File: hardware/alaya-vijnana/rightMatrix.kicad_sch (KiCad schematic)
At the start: 42 parts, among them SW24 MX HotSwap, SW25 MX HotSwap, SW26 MX HotSwap, SW27 MX HotSwap, SW28 MX HotSwap, SW29 MX HotSwap, SW30 MX HotSwap, SW31 MX HotSwap, SW32 MX HotSwap, SW33 MX HotSwap, SW34 MX HotSwap, SW35 MX HotSwap, SW36 MX HotSwap, SW37 MX HotSwap, SW38 MX HotSwap, SW39 MX HotSwap, SW40 MX HotSwap, SW41 MX HotSwap, SW42 MX HotSwap, SW43 MX HotSwap, SW44 MX HotSwap

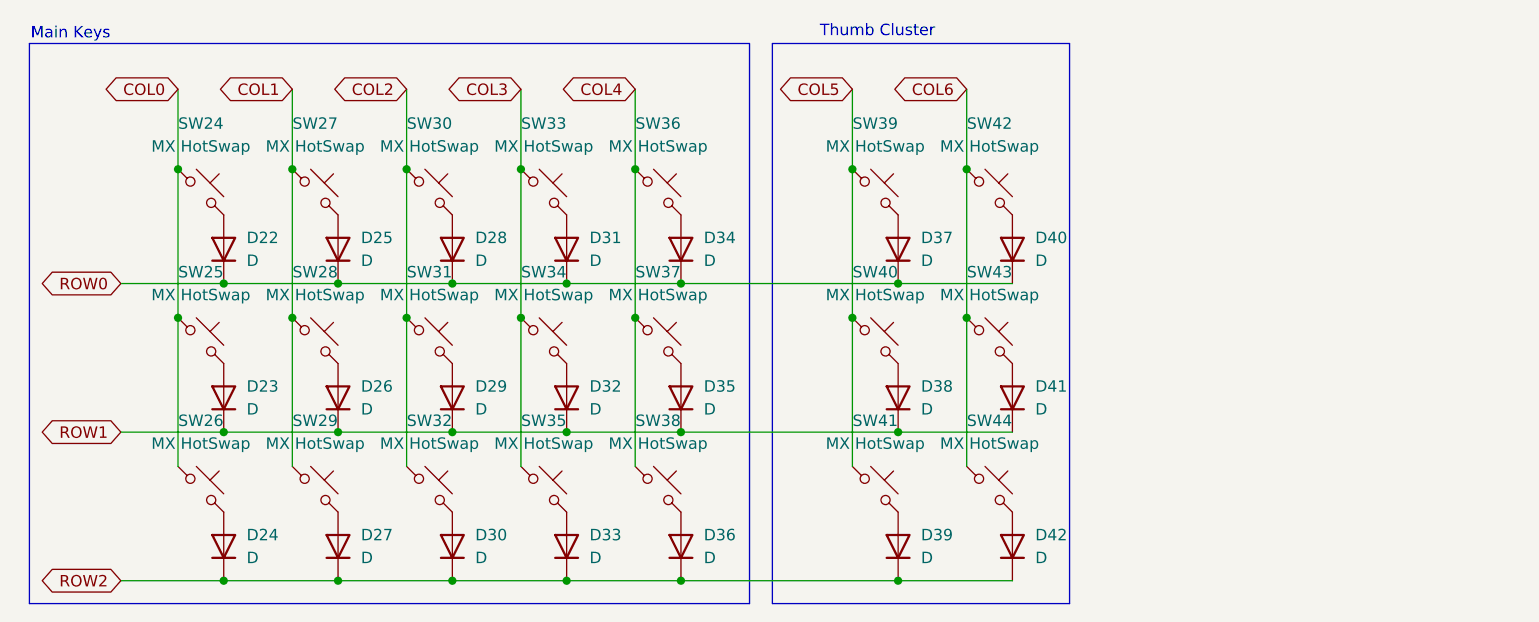
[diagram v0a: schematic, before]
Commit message: finished key wiring w/ connectors
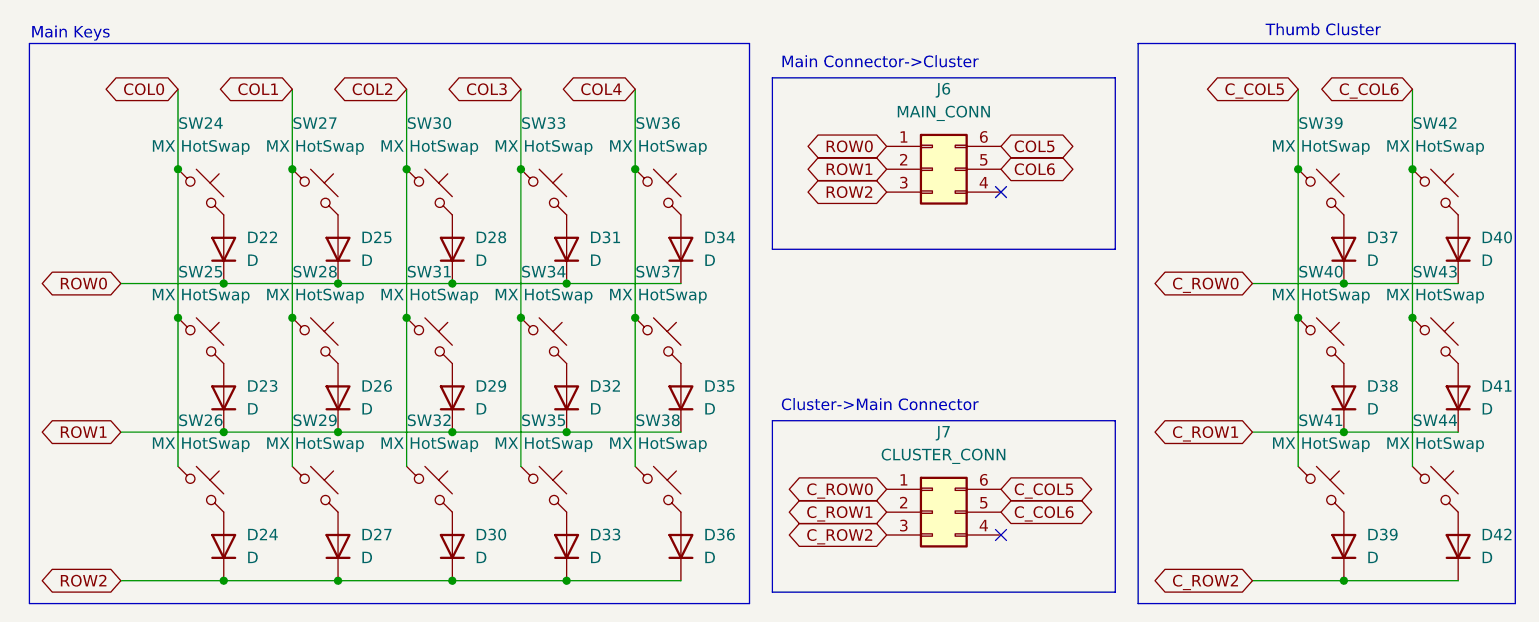
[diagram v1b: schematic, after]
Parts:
- added J6: MAIN_CONN, Connector_IDC:IDC-Header_2x03_P2.54mm_Horizontal, symbol Connector_Generic:Conn_02x03_Counter_Clockwise
- added J7: CLUSTER_CONN, Connector_IDC:IDC-Header_2x03_P2.54mm_Horizontal, symbol Connector_Generic:Conn_02x03_Counter_Clockwise
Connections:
- net COL5: now also J6.6 (Pin_6); no longer SW39.1, SW40.1, SW41.1
- net COL6: now also J6.5 (Pin_5); no longer SW42.1, SW43.1, SW44.1
- net ROW0: now also J6.1 (Pin_1); no longer D37.1 (K), D40.1 (K)
- net ROW1: now also J6.2 (Pin_2); no longer D38.1 (K), D41.1 (K)
- net ROW2: now also J6.3 (Pin_3); no longer D39.1 (K), D42.1 (K)
- new net C_COL5: J7.6 (Pin_6), SW39.1, SW40.1, SW41.1
- new net C_COL6: J7.5 (Pin_5), SW42.1, SW43.1, SW44.1
- new net C_ROW0: D37.1 (K), D40.1 (K), J7.1 (Pin_1)
- new net C_ROW1: D38.1 (K), D41.1 (K), J7.2 (Pin_2)
- new net C_ROW2: D39.1 (K), D42.1 (K), J7.3 (Pin_3)
- no-connect marks 0 -> 2
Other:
- note added: "Cluster->Main Connector"
- note added: "Main Connector->Cluster"
- moved on the sheet: D37, D38, D39, D40, D41, D42, SW39, SW40, SW41, SW42, SW43, SW44
